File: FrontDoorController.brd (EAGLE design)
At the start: 31.4 x 49.1 mm, 10 parts

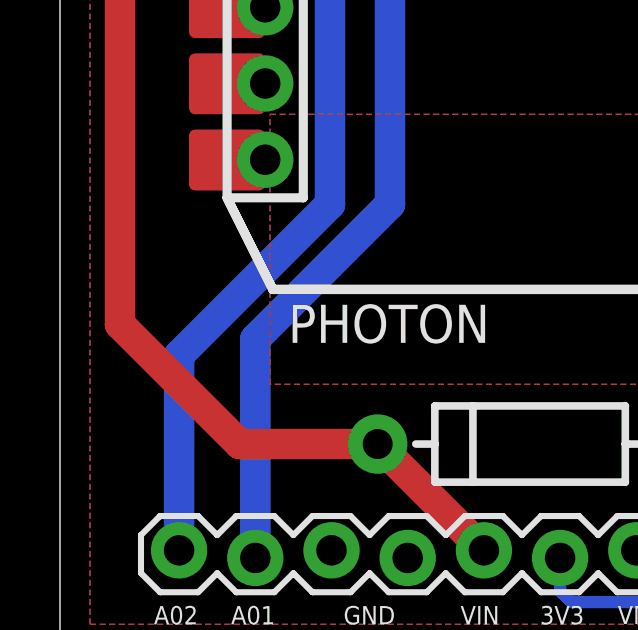
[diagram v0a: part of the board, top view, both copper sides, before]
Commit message: Door_Control_PCB: Add Particle Logo
Add the Particle (Spark) logo to the board to make it cooler looking and
more official (not at all official).
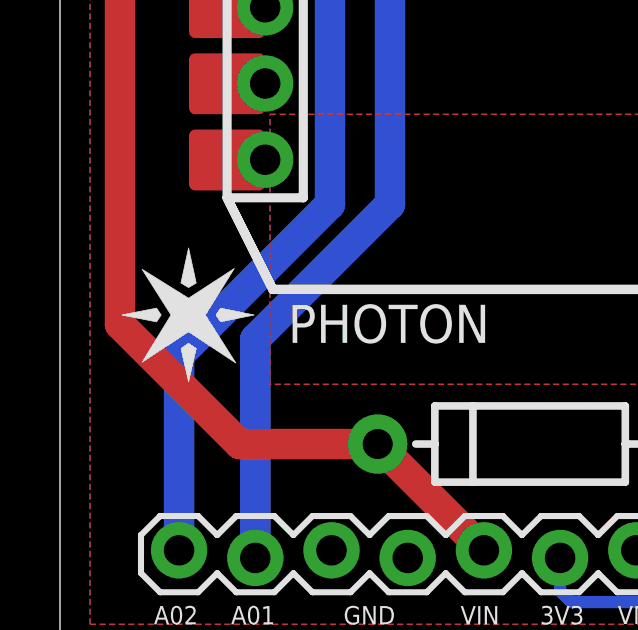
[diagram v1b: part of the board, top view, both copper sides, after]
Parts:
- added U$1: SPARK_LOGOLARGE, Mikes-Stuff:SPARK_LOGO
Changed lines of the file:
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@@
 <element name="PHOTON" library="Spark" package="PHOTON_SMD" value="PHOTON_SMD" x="5.57" y="12.16" smashed="yes">
 <attribute name="NAME" x="7.602" y="10.382" size="1.27" layer="25" ratio="10"/>
-<attribute name="VALUE" x="7.602" y="8.858" size="1.27" layer="27"/>
 </element>
 <element name="FRAME1" library="SparkFun-Aesthetics" package="CREATIVE_COMMONS" value="FRAME-LETTER" x="87" y="34"/>
@@
 <element name="U$3" library="Spark" package="PHOTON" value="PHOTON_WITH_HEADERS" x="5.57" y="12.17" smashed="yes"/>
 <element name="R1" library="SparkFun-Resistors" package="0603-RES" value="1K" x="21.5" y="21.69" rot="MR180"/>
+<element name="U$1" library="Mikes-Stuff" package="SPARK_LOGO" value="SPARK_LOGOLARGE" x="2" y="9"/>
 </elements>
 <signals>
